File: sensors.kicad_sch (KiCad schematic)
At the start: 11 parts, among them J4 Conn_01x05_Pin, U12 CY15B064J-SXET, U3 MMC5983MA, U4 BMI088, U9 MCP23009-E/MG

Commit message: v0.2
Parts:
- removed J4: Conn_01x05_Pin, Connector_PinHeader_2.00mm:PinHeader_1x04_P2.00mm_Vertical, symbol Connector:Conn_01x04_Pin
- removed U9: MCP23009-E/MG, QFN16_3x3MC_MCH, symbol MCP23009-E:MCP23009-E_MG
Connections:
- no-connect marks 11 -> 8
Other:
- title: RT1050 DevBoard for Project Horizon -> Payload Board for Pleiades Atlas
- moved on the sheet: C50, C51, C52, C62, R4, R5, U12, U3, U4

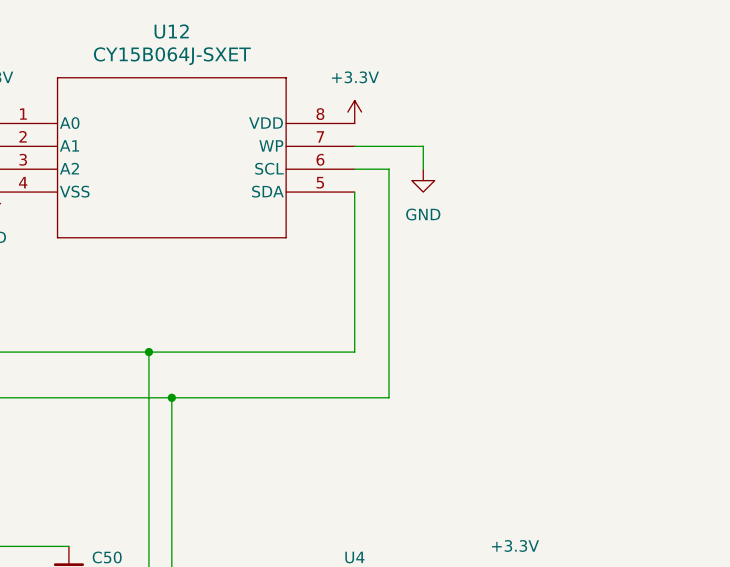
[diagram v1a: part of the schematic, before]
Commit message: added testpoints
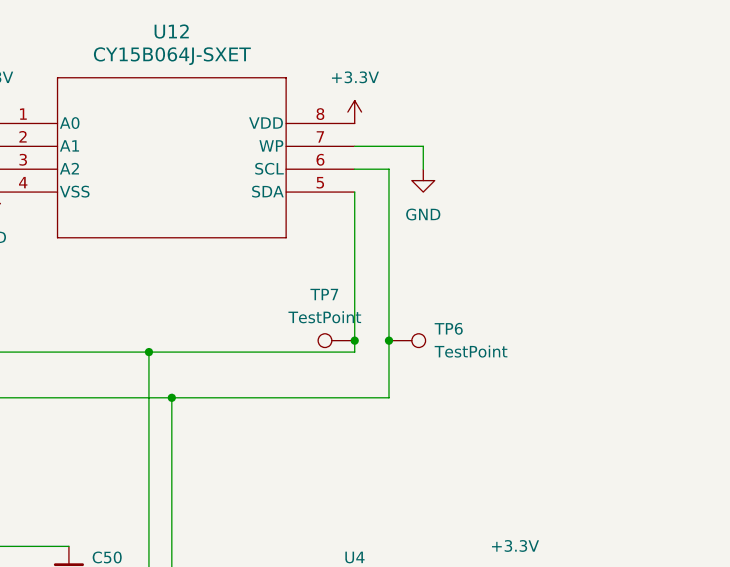
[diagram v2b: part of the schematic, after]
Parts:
- added TP6, TP7: TestPoint, TestPoint:TestPoint_Pad_D1.5mm, symbol Connector:TestPoint
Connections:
- net LPI2C1_SCL: now also TP6.1
- net LPI2C1_SDA: now also TP7.1
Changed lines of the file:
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@@
+	)
+	(junction
+		(at 148.59 54.61)
+		(diameter 0)
+		(color 0 0 0 0)
 	)
 	(junction
@@
 	)
 	(junction
+		(at 144.78 54.61)
+		(diameter 0)
+		(color 0 0 0 0)
+	)
+	(junction
 		(at 54.61 60.96)
 		(diameter 0)
@@
 	(wire
 		(pts
+			(xy 144.78 54.61) (xy 144.78 55.88)
+		)
+		(stroke
+			(width 0)
+			(type default)
+		)
+	)
+	(wire
+		(pts
 			(xy 50.8 55.88) (xy 121.92 55.88)
 		)
@@
 	(wire
 		(pts
-			(xy 144.78 38.1) (xy 144.78 55.88)
+			(xy 144.78 38.1) (xy 144.78 54.61)
 		)
 		(stroke
@@
 	(wire
 		(pts
+			(xy 148.59 54.61) (xy 148.59 60.96)
+		)
+		(stroke
+			(width 0)
+			(type default)
+		)
+	)
+	(wire
+		(pts
 			(xy 54.61 85.09) (xy 54.61 60.96)
 		)
@@
 	(wire
 		(pts
-			(xy 148.59 35.56) (xy 148.59 60.96)
+			(xy 148.59 35.56) (xy 148.59 54.61)
 		)
 		(stroke
@@
 	)
 	(symbol
+		(lib_id "Connector:TestPoint")
+		(at 148.59 54.61 270)
+		(unit 1)
+		(exclude_from_sim no)
+		(in_bom yes)
+		(on_board yes)
+		(dnp no)
+		(fields_autoplaced yes)
+		(property "Reference" "TP6"
+			(at 153.67 53.3399 90)
+			(effects
+				(font
+					(size 1.27 1.27)
+				)
+				(justify left)
+			)
+		)
+		(property "Value" "TestPoint"
+			(at 153.67 55.8799 90)
+			(effects
+				(font
+					(size 1.27 1.27)
+				)
+				(justify left)
+			)
+		)
+		(property "Footprint" "TestPoint:TestPoint_Pad_D1.5mm"
+			(at 148.59 59.69 0)
+			(effects
+				(font
+					(size 1.27 1.27)
+				)
+				(hide yes)
+			)
+		)
+		(property "Datasheet" "~"
+			(at 148.59 59.69 0)
+			(effects
+				(font
+					(size 1.27 1.27)
+				)
+				(hide yes)
+			)
+		)
+		(property "Description" "test point"
+			(at 148.59 54.61 0)
+			(effects
+				(font
+					(size 1.27 1.27)
+				)
+				(hide yes)
+			)
+		)
+		(pin "1"
+		)
+		(instances
+			(project "RT1050"
+				(path "/dd9d031d-43a1-4442-b493-27451a14e0d9/2d6e0293-1e7f-4e64-b0be-64f8e31d184d"
+					(reference "TP6")
+					(unit 1)
+				)
+			)
+		)
+	)
+	(symbol
 		(lib_id "power:GND")
 		(at 172.72 96.52 0)
@@
 					(unit 1)
 				)
+			)
+		)
+	)
+	(symbol
+		(lib_id "Connector:TestPoint")
+		(at 144.78 54.61 90)
+		(unit 1)
+		(exclude_from_sim no)
+		(in_bom yes)
+		(on_board yes)
+		(dnp no)
+		(fields_autoplaced yes)
+		(property "Reference" "TP7"
+			(at 141.478 49.53 90)
+			(effects
+				(font
+					(size 1.27 1.27)
+				)
+			)
+		)
+		(property "Value" "TestPoint"
+			(at 141.478 52.07 90)
+			(effects
+				(font
+					(size 1.27 1.27)
+				)
+			)
+		)
+		(property "Footprint" "TestPoint:TestPoint_Pad_D1.5mm"
+			(at 144.78 49.53 0)
+			(effects
+				(font
+					(size 1.27 1.27)
+				)
+				(hide yes)
+			)
+		)
+		(property "Datasheet" "~"
+			(at 144.78 49.53 0)
+			(effects
+				(font
+					(size 1.27 1.27)
+				)
+				(hide yes)
+			)
+		)
+		(property "Description" "test point"
+			(at 144.78 54.61 0)
+			(effects
+				(font
+					(size 1.27 1.27)
+				)
+				(hide yes)
+			)
+		)
+		(pin "1"
+		)
+		(instances
+			(project "RT1050"
+				(path "/dd9d031d-43a1-4442-b493-27451a14e0d9/2d6e0293-1e7f-4e64-b0be-64f8e31d184d"
+					(reference "TP7")
+					(unit 1)
+				)
